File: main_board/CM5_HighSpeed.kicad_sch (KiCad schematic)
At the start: 16 parts, among them J1 USB3_A, J10 Conn_01x22_Female, J11 501568-0607-TR325, J12 SM04B-XSRS-ETBLFSN, J13 SM10B-XSRS-ETB, J22 690-019-298-412, U12 RT9742SNGV, U6 AP22653W6

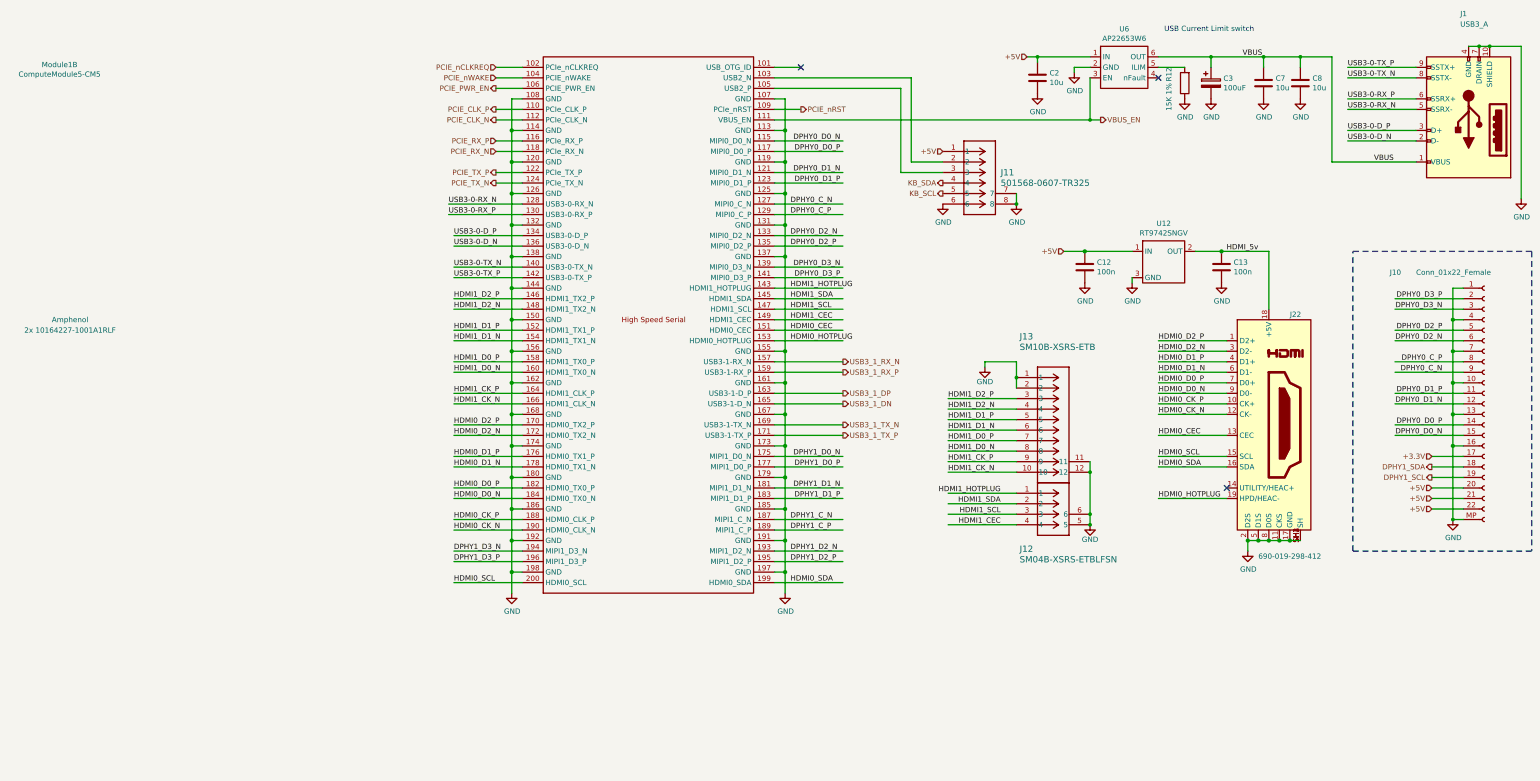
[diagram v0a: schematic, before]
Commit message: Fix critical problems
- Adding USB2 hub on USB3 port did not work correctly
- PM I2C bus was not working when CM5 is shut down
- Missing OTG ID pin
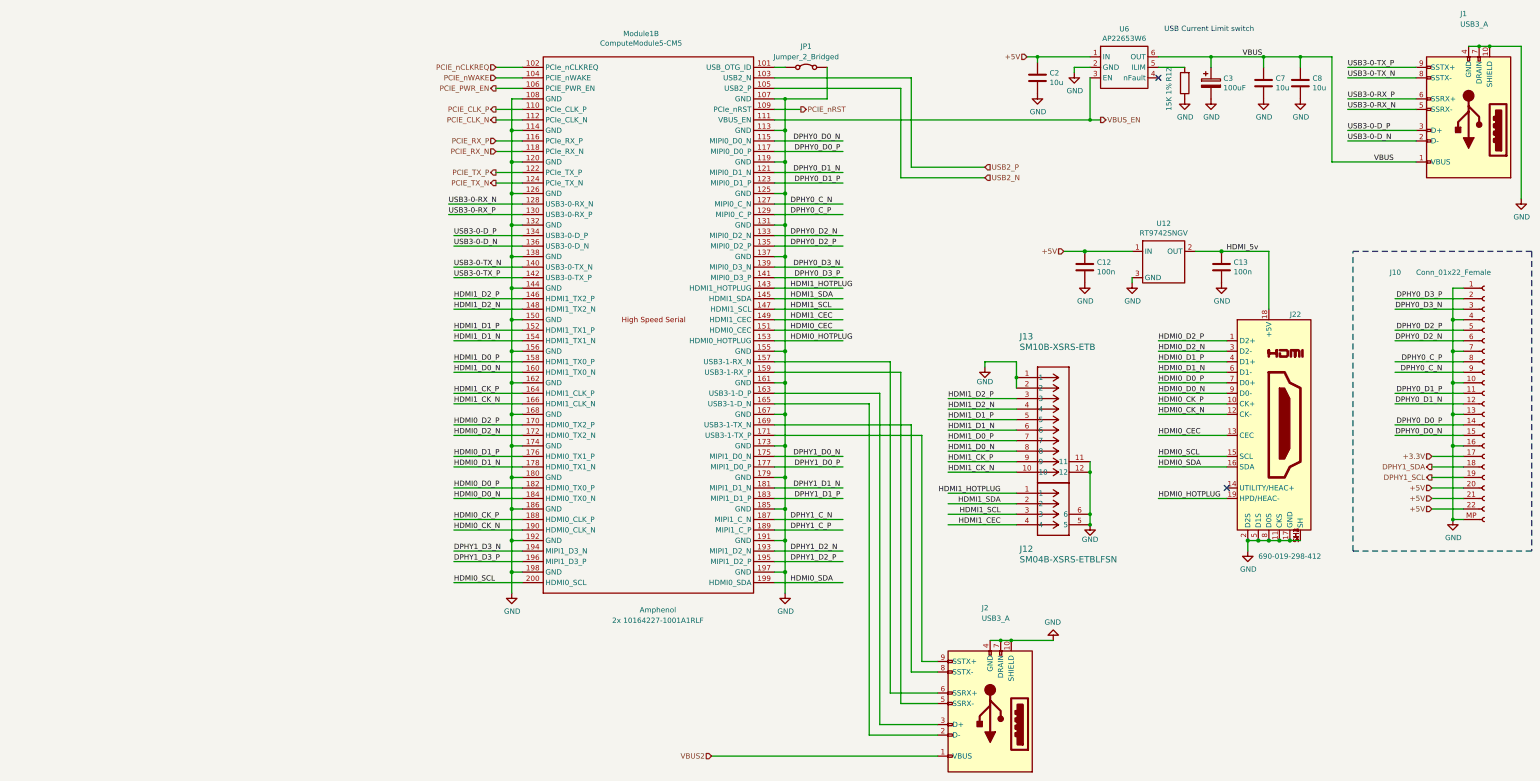
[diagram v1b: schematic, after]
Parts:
- removed J11: 501568-0607-TR325, CONN_501568-0607-TR325_MOL, symbol 000_Custom:501568-0607-TR325
- added J2: USB3_A, 000_custom:U3BU1ASMT1, symbol Connector:USB3_A
- added JP1: Jumper_2_Bridged, symbol Jumper:Jumper_2_Bridged
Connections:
- net GND: now also J2.10 (SHIELD), J2.4 (GND), J2.7 (DRAIN), JP1.2 (B)
- net at Module1.101 (USB_OTG_ID): now also JP1.1 (A)
- net USB2_P: now reaches Module1.103 (USB2_N)
- net USB2_N: now reaches Module1.105 (USB2_P)
- net USB3_1_DN: no longer names the net of Module1.165 (USB3-1-D_N)
- net USB3_1_DN: now also J2.2 (D-)
- net USB3_1_DP: no longer names the net of Module1.163 (USB3-1-D_P)
- net USB3_1_DP: now also J2.3 (D+)
- net USB3_1_RX_N: no longer names the net of Module1.157 (USB3-1-RX_N)
- net USB3_1_RX_N: now also J2.6 (SSRX+)
- net USB3_1_RX_P: no longer names the net of Module1.159 (USB3-1-RX_P)
- net USB3_1_RX_P: now also J2.5 (SSRX-)
- net USB3_1_TX_N: no longer names the net of Module1.169 (USB3-1-TX_N)
- net USB3_1_TX_N: now also J2.8 (SSTX-)
- net USB3_1_TX_P: no longer names the net of Module1.171 (USB3-1-TX_P)
- net USB3_1_TX_P: now also J2.9 (SSTX+)
- new net VBUS2: J2.1 (VBUS)
- no-connect marks 3 -> 2

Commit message: Fix CM5 not waking up when enabling boost
When battery is fully charged, CM5 does not turn on.
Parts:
- JP1: footprint (none) -> Jumper:SolderJumper-2_P1.3mm_Bridged2Bar_RoundedPad1.0x1.5mm
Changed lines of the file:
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@@
 			)
 		)
-		(property "Footprint" ""
+		(property "Footprint" "Jumper:SolderJumper-2_P1.3mm_Bridged2Bar_RoundedPad1.0x1.5mm"
 			(at 106.68 25.4 0)
 			(effects
